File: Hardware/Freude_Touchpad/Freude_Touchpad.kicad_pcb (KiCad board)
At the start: 4 copper layers, 26.4 x 26.4 mm, 9 parts, among them J1 Conn_01x06_Female, U1 IQS572

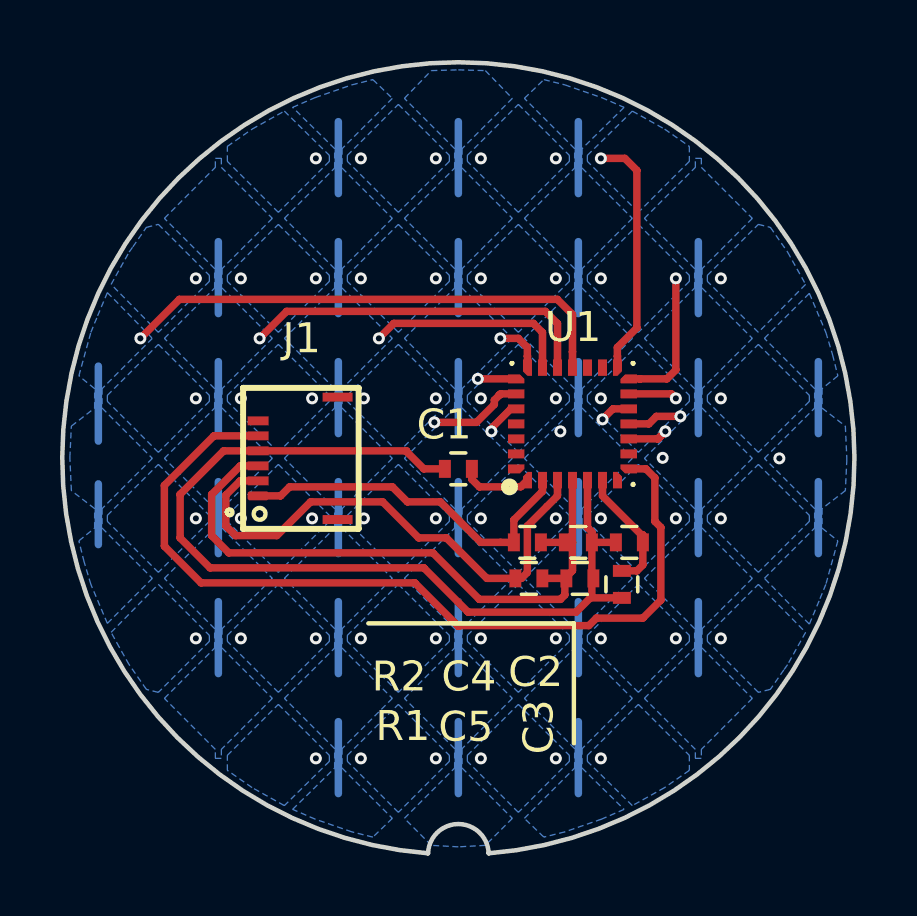
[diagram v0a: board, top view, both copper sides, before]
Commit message: change hole size to 0.45mm, decrease soldermask expansion
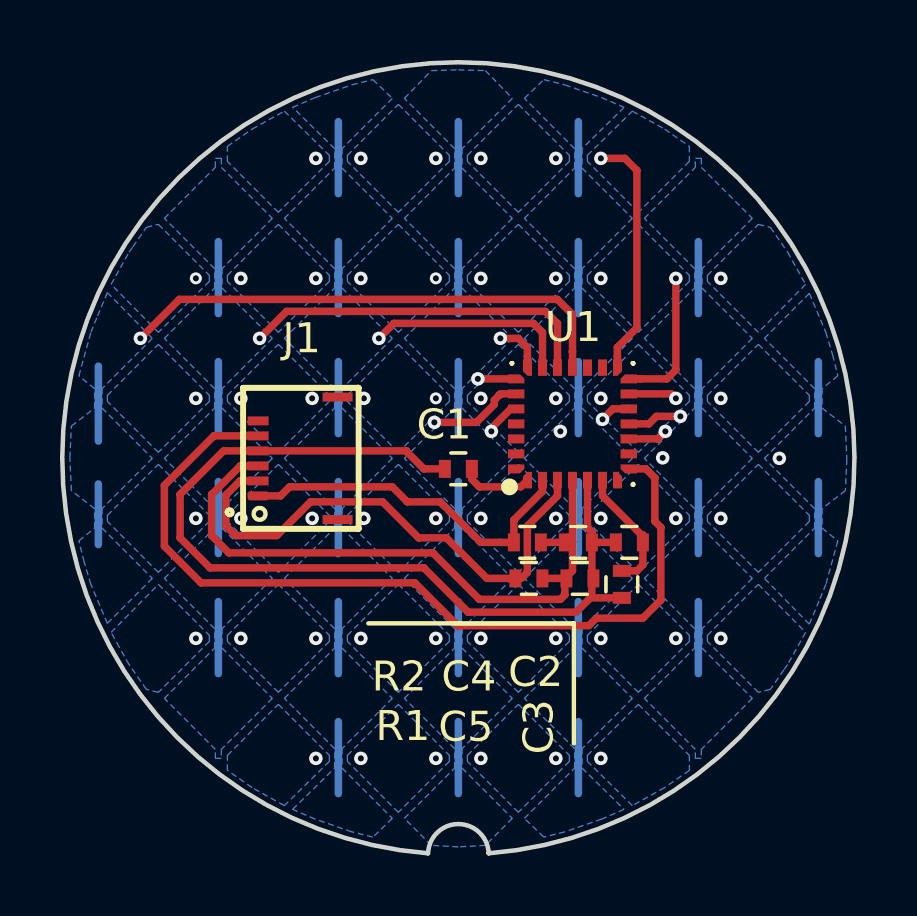
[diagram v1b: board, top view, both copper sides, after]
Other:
- rule via_min_size: 0.4 -> 0.45

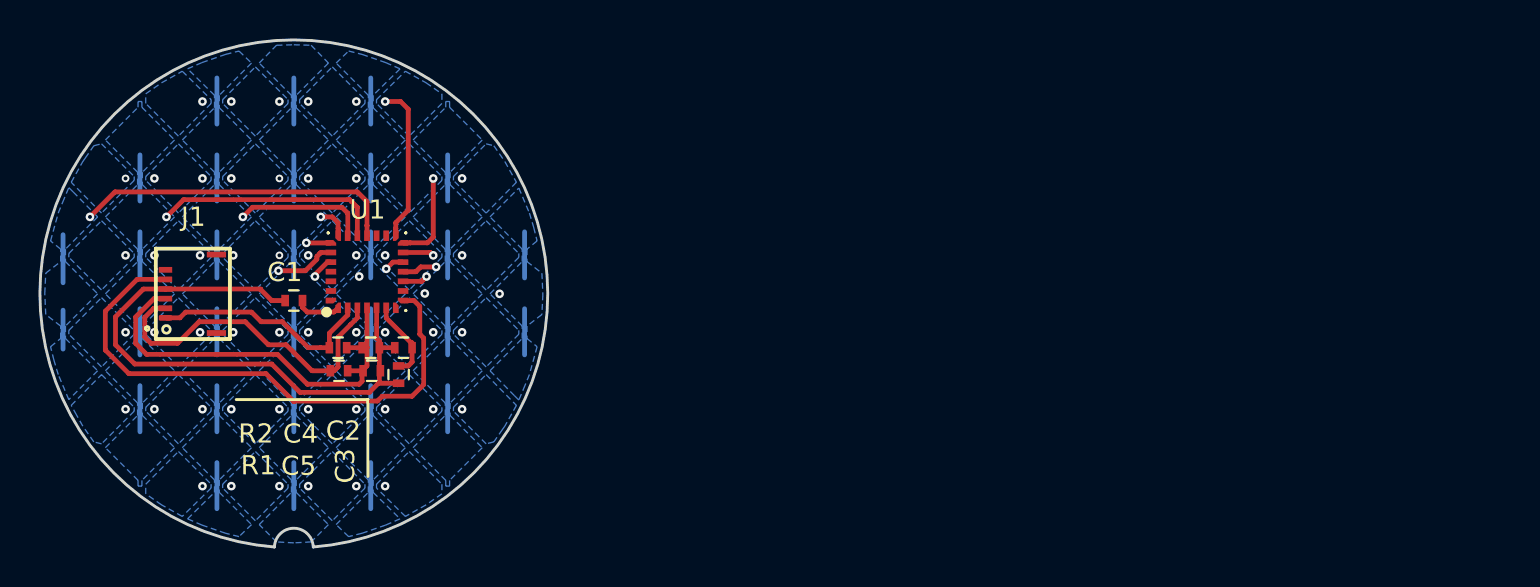
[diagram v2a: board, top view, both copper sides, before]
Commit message: added ground pour and ground ring
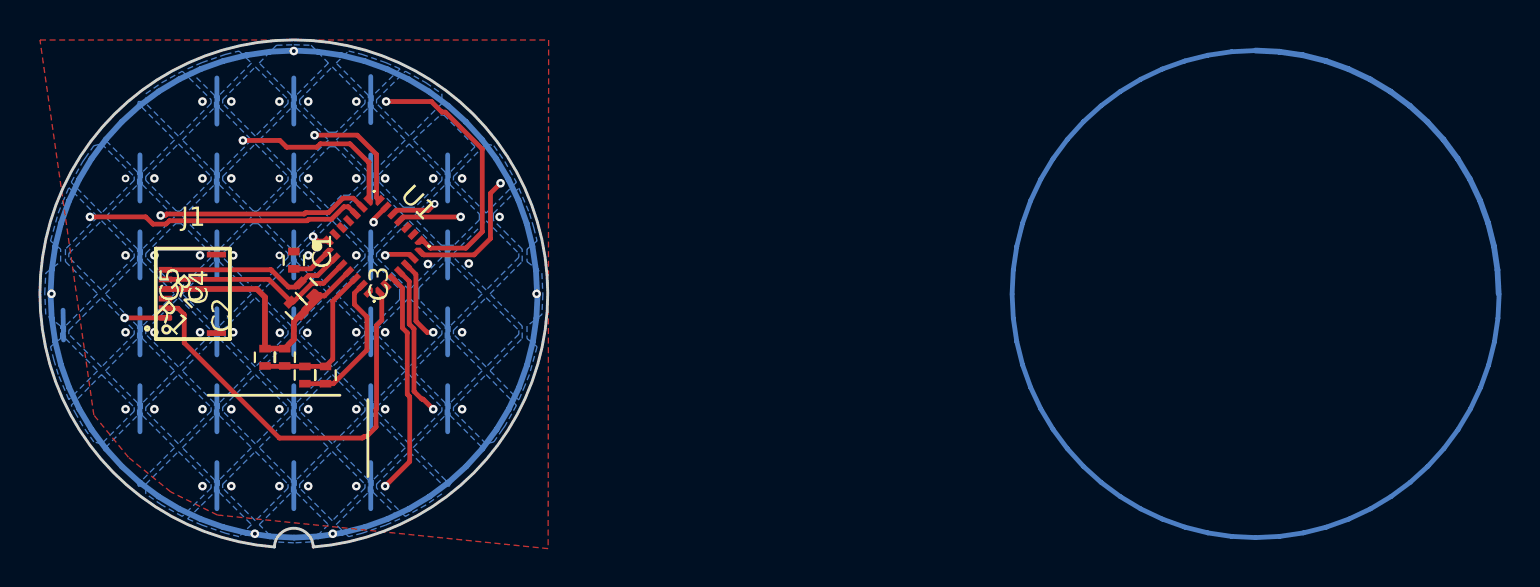
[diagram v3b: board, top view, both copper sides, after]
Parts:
- moved C5 5.59 mm to (98.5, 103.3), turned to 90 degrees
- moved C2 5.32 mm to (100.6, 104.2), turned to 270 degrees
- moved C4 4.50 mm to (99.5, 103.3), turned to 90 degrees
- moved R1 3.94 mm to (100.1, 100.8), turned to 135 degrees
- moved C3 3.80 mm to (101.7, 104.2), turned to 270 degrees
- moved R2 3.47 mm to (100.7, 99.8), turned to 135 degrees
- moved C1 2.10 mm to (100.0, 98.2), turned to 90 degrees
- moved U1 1.38 mm to (104.2, 97.5), turned to 45 degrees
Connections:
- C1 pad 1: Net-(C1-Pad1) -> /NRST
- J1 pad 0: (no net) -> GNDA
- J1 pad 1: /SDA_TP -> /SW_IN
- J1 pad 2: /SCL_TP -> /RDY_TP
- J1 pad 3: +3.3VA -> GNDA
- J1 pad 4: GNDA -> +3.3VA
- J1 pad 5: /RDY_TP -> /SCL_TP
- J1 pad 6: Net-(J1-Pad6) -> /SDA_TP
- U1 pad 1: Net-(U1-Pad1) -> /NRST
- U1 pad 16: Net-(U1-Pad16) -> GNDA
- U1 pad 17: Net-(U1-Pad17) -> GNDA
- U1 pad 18: XA00 -> XA06
- U1 pad 19: XA01 -> XA05
- U1 pad 20: XA02 -> XA04
- U1 pad 22: XA04 -> XA02
- U1 pad 23: XA05 -> XA01
- U1 pad 24: XA06 -> XA00
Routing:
- net GNDA: track 32.0 -> 389.8 mm, vias 0 -> 5
- net (no net): track 0.00 -> 79.5 mm
- net /SW_IN: track 0.00 -> 18.1 mm, vias 0 -> 2
- net XA06: track 15.9 -> 5.28 mm
- net XA05: track 20.9 -> 12.0 mm, vias 2 -> 1
- net /SCL_TP: track 17.6 -> 10.5 mm
- net /RDY_TP: track 29.0 -> 22.0 mm
- net +3.3VA: track 21.8 -> 14.9 mm
- net YA05: track 12.7 -> 18.6 mm
- net XA00: track 21.5 -> 16.0 mm
- net XA03: track 16.1 -> 20.5 mm
- net XA04: track 19.6 -> 15.4 mm, vias 2 -> 1
- net YA01: track 19.1 -> 15.4 mm, vias 11 -> 10
- net Net-(C2-Pad2): track 4.24 -> 7.75 mm
- net YA04: track 12.2 -> 14.7 mm, vias 10 -> 11
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- added copper zone on F.Cu, net GNDA
- added copper zone on In2.Cu, net GNDA
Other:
- net class Default: via_dia 0.4 -> 0.45

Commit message: resolves 10, resolves 9, resolves 6, resolves 5, add ground ring around touch sensor, add ground ring on top, separate RX from TX and include ground plane between
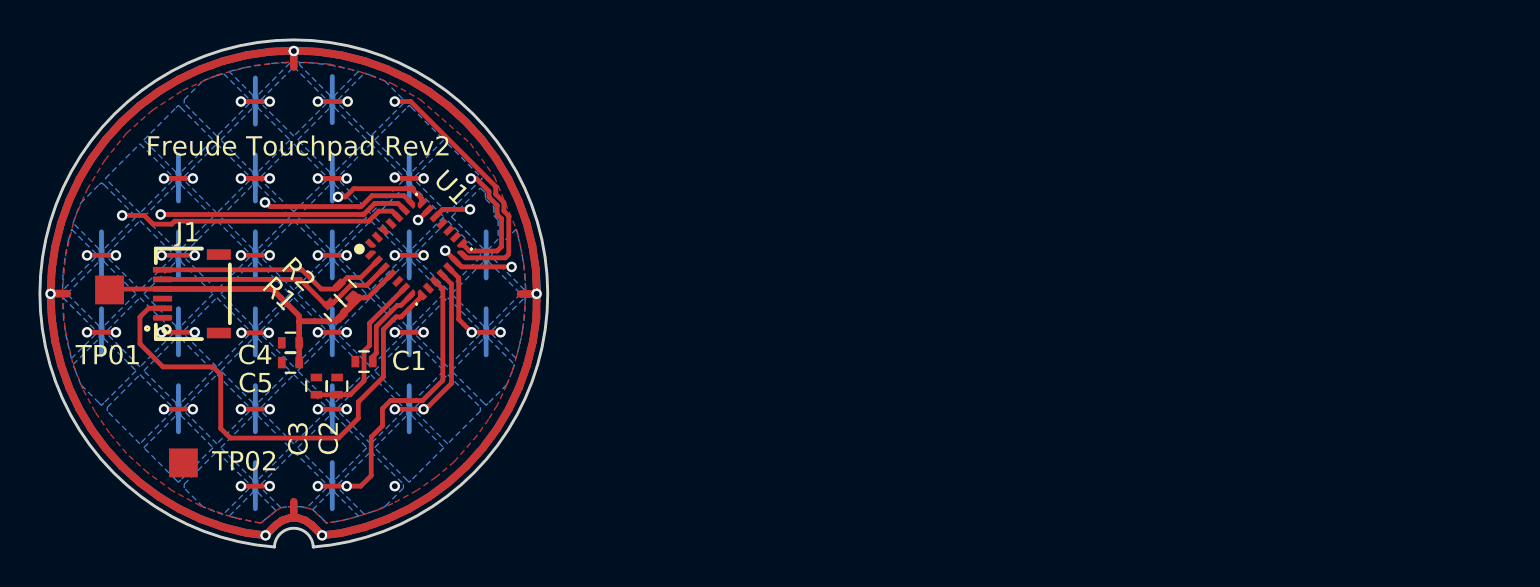
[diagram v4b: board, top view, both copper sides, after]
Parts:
- added TP01: Measurement_Point_Square-SMD-Pad_Small, Measurement_Points:Measurement_Point_Square-SMD-Pad_Small, F.Cu at (90.4, 99.8)
- added TP02: Measurement_Point_Square-SMD-Pad_Small, Measurement_Points:Measurement_Point_Square-SMD-Pad_Small, F.Cu at (94.3, 108.8)
- moved C1 6.41 mm to (103.7, 103.5), turned to 180 degrees
- moved U1 2.21 mm to (106.4, 97.7)
- moved R1 2.03 mm to (102.2, 100.8)
- moved R2 2.03 mm to (102.7, 99.8)
- moved C2 1.77 mm to (102.2, 104.8)
- moved C5 1.35 mm to (99.8, 103.6), turned to 0 degrees
- moved C4 0.81 mm to (99.8, 102.5), turned to 0 degrees
- moved C3 0.75 mm to (101.2, 104.8)
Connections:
- J1 pad 1: /SW_IN -> Net-(J1-Pad1)
- U1 pad 1: /NRST -> (no net)
- U1 pad 14: YA04 -> YA05
- U1 pad 15: YA05 -> YA04
- U1 pad 18: XA06 -> (no net)
- U1 pad 7: (no net) -> /NRST
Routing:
- net GNDA: track 389.8 -> 163.5 mm
- net (no net): track 79.5 -> 0.00 mm
- net /SW_IN: track 18.1 -> 0.00 mm, vias 2 -> 0
- net XA06: track 5.28 -> 0.00 mm, vias 2 -> 0
- net XA05: track 12.0 -> 6.77 mm
- net XA04: track 15.4 -> 10.4 mm
- net /RDY_TP: track 22.0 -> 26.2 mm
- net +3.3VA: track 14.9 -> 19.0 mm
- net XA00: track 16.0 -> 19.7 mm
- net /NRST: track 2.17 -> 4.41 mm
- net /SCL_TP: track 10.5 -> 12.7 mm
- net /SDA_TP: track 10.1 -> 12.2 mm
- net YA05: track 18.6 -> 16.5 mm, vias 6 -> 5
- net YA04: track 14.7 -> 12.7 mm, vias 11 -> 9
- net XA01: track 20.6 -> 22.7 mm
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- removed copper zone on In2.Cu, net GNDA
- removed copper zone on B.Cu, net XA06
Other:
- copper layers 4 -> 2
- board text added: "Freude Touchpad Rev2"
